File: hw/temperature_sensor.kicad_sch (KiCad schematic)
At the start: 8 parts, among them U103 DS18B20

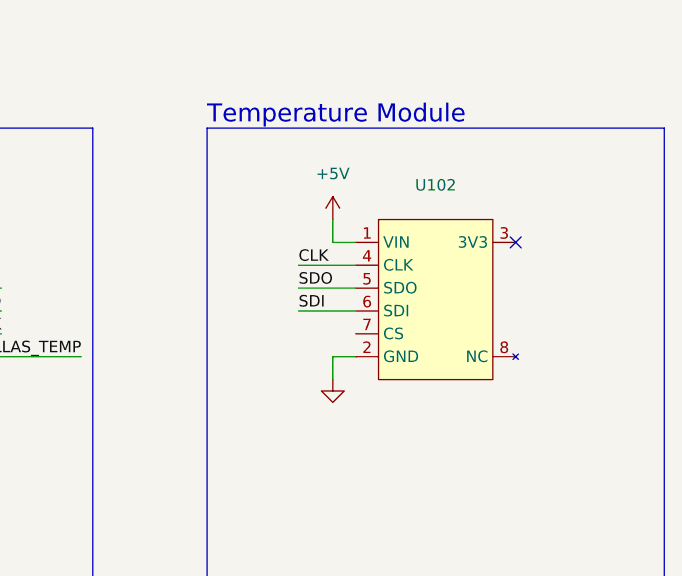
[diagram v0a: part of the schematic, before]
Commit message: schematic corrections & pcb routed
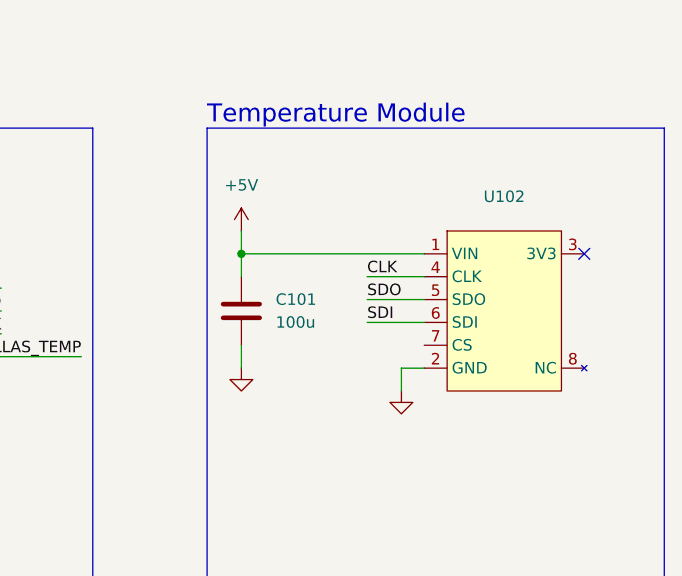
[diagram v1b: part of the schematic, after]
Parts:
- added C101: 100u, Capacitor_THT:CP_Radial_D5.0mm_P2.50mm, symbol Device:C
- U103: footprint Package_TO_SOT_THT:TO-92_Inline -> Connector_PinHeader_2.54mm:PinHeader_1x03_P2.54mm_Horizontal
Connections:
- net +5V: now also C101.1
- net GND: now also C101.2
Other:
- moved on the sheet: U102
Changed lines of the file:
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@@
 	(paper "A4")
+	(junction
+		(at 92.71 77.47)
+		(diameter 0)
+		(color 0 0 0 0)
+	)
 	(junction
 		(at 54.61 149.86)
@@
 	)
 	(no_connect
-		(at 123.19 76.2)
+		(at 130.81 77.47)
 	)
 	(no_connect
@@
 	(wire
 		(pts
-			(xy 99.06 78.74) (xy 105.41 78.74)
-		)
-		(stroke
-			(width 0)
-			(type default)
-		)
-	)
-	(wire
-		(pts
-			(xy 99.06 81.28) (xy 105.41 81.28)
+			(xy 106.68 80.01) (xy 113.03 80.01)
+		)
+		(stroke
+			(width 0)
+			(type default)
+		)
+	)
+	(wire
+		(pts
+			(xy 92.71 90.17) (xy 92.71 87.63)
+		)
+		(stroke
+			(width 0)
+			(type default)
+		)
+	)
+	(wire
+		(pts
+			(xy 92.71 77.47) (xy 113.03 77.47)
+		)
+		(stroke
+			(width 0)
+			(type default)
+		)
+	)
+	(wire
+		(pts
+			(xy 106.68 82.55) (xy 113.03 82.55)
 		)
 		(stroke
@@
 	(wire
 		(pts
-			(xy 102.87 73.66) (xy 102.87 76.2)
-		)
-		(stroke
-			(width 0)
-			(type default)
-		)
-	)
-	(wire
-		(pts
 			(xy 44.45 160.02) (xy 44.45 157.48)
 		)
@@
 	(wire
 		(pts
+			(xy 92.71 77.47) (xy 92.71 74.93)
+		)
+		(stroke
+			(width 0)
+			(type default)
+		)
+	)
+	(wire
+		(pts
 			(xy 62.23 76.2) (xy 59.69 76.2)
 		)
@@
 	(wire
 		(pts
-			(xy 102.87 91.44) (xy 102.87 88.9)
+			(xy 110.49 92.71) (xy 110.49 90.17)
 		)
 		(stroke
@@
 	(wire
 		(pts
-			(xy 99.06 83.82) (xy 105.41 83.82)
-		)
-		(stroke
-			(width 0)
-			(type default)
-		)
-	)
-	(wire
-		(pts
-			(xy 102.87 88.9) (xy 105.41 88.9)
+			(xy 106.68 85.09) (xy 113.03 85.09)
+		)
+		(stroke
+			(width 0)
+			(type default)
+		)
+	)
+	(wire
+		(pts
+			(xy 110.49 90.17) (xy 113.03 90.17)
 		)
 		(stroke
@@
 	(wire
 		(pts
+			(xy 92.71 77.47) (xy 92.71 80.01)
+		)
+		(stroke
+			(width 0)
+			(type default)
+		)
+	)
+	(wire
+		(pts
 			(xy 59.69 81.28) (xy 66.04 81.28)
 		)
@@
 		(pts
 			(xy 39.37 73.66) (xy 39.37 76.2)
-		)
-		(stroke
-			(width 0)
-			(type default)
-		)
-	)
-	(wire
-		(pts
-			(xy 102.87 76.2) (xy 105.41 76.2)
 		)
 		(stroke
@@
 	)
 	(label "CLK"
-		(at 99.06 78.74 0)
+		(at 106.68 80.01 0)
 		(effects
 			(font
@@
 	)
 	(label "SDO"
-		(at 99.06 81.28 0)
+		(at 106.68 82.55 0)
 		(effects
 			(font
@@
 	)
 	(label "SDI"
-		(at 99.06 83.82 0)
+		(at 106.68 85.09 0)
 		(effects
 			(font
@@
 			)
 		)
-		(property "Footprint" "Package_TO_SOT_THT:TO-92_Inline"
+		(property "Footprint" "Connector_PinHeader_2.54mm:PinHeader_1x03_P2.54mm_Horizontal"
 			(at 19.05 156.21 0)
 			(effects
@@
 	(symbol
 		(lib_id "power:+5V")
-		(at 102.87 73.66 0)
+		(at 92.71 74.93 0)
 		(unit 1)
 		(exclude_from_sim no)
@@
 		(fields_autoplaced yes)
 		(property "Reference" "#PWR0104"
-			(at 102.87 77.47 0)
+			(at 92.71 78.74 0)
 			(effects
 				(font
@@
 		)
 		(property "Value" "+5V"
-			(at 102.87 68.58 0)
+			(at 92.71 69.85 0)
 			(effects
 				(font
@@
 		)
 		(property "Footprint" ""
-			(at 102.87 73.66 0)
+			(at 92.71 74.93 0)
 			(effects
 				(font
@@
 		)
 		(property "Datasheet" ""
-			(at 102.87 73.66 0)
+			(at 92.71 74.93 0)
 			(effects
 				(font
@@
 		)
 		(property "Description" "Power symbol creates a global label with name \"+5V\""
-			(at 102.87 73.66 0)
+			(at 92.71 74.93 0)
 			(effects
 				(font
@@
 	(symbol
 		(lib_id "power:GND")
-		(at 102.87 91.44 0)
+		(at 110.49 92.71 0)
 		(unit 1)
 		(exclude_from_sim no)
@@
 		(fields_autoplaced yes)
 		(property "Reference" "#PWR0105"
-			(at 102.87 97.79 0)
+			(at 110.49 99.06 0)
 			(effects
 				(font
@@
 		)
 		(property "Value" "GND"
-			(at 102.87 96.52 0)
+			(at 110.49 97.79 0)
 			(effects
 				(font
@@
 		)
 		(property "Footprint" ""
-			(at 102.87 91.44 0)
+			(at 110.49 92.71 0)
 			(effects
 				(font
@@
 		)
 		(property "Datasheet" ""
-			(at 102.87 91.44 0)
+			(at 110.49 92.71 0)
 			(effects
 				(font
@@
 		)
 		(property "Description" "Power symbol creates a global label with name \"GND\" , ground"
-			(at 102.87 91.44 0)
+			(at 110.49 92.71 0)
 			(effects
 				(font
@@
 				(path "/d1c078f0-e8c6-4381-8df5-9bbdd95d8ece"
 					(reference "#PWR0105")
+					(unit 1)
+				)
+			)
+		)
+	)
+	(symbol
+		(lib_id "Device:C")
+		(at 92.71 83.82 0)
+		(unit 1)
+		(exclude_from_sim no)
+		(in_bom yes)
+		(on_board yes)
+		(dnp no)
+		(fields_autoplaced yes)
+		(property "Reference" "C101"
+			(at 96.52 82.5499 0)
+			(effects
+				(font
+					(size 1.27 1.27)
+				)
+				(justify left)
+			)
+		)
+		(property "Value" "100u"
+			(at 96.52 85.0899 0)
+			(effects
+				(font
+					(size 1.27 1.27)
+				)
+				(justify left)
+			)
+		)
+		(property "Footprint" "Capacitor_THT:CP_Radial_D5.0mm_P2.50mm"
+			(at 93.6752 87.63 0)
+			(effects
+				(font
+					(size 1.27 1.27)
+				)
+				(hide yes)
+			)
+		)
+		(property "Datasheet" "~"
+			(at 92.71 83.82 0)
+			(effects
+				(font
+					(size 1.27 1.27)
+				)
+				(hide yes)
+			)
+		)
+		(property "Description" "Unpolarized capacitor"
+			(at 92.71 83.82 0)
+			(effects
+				(font
+					(size 1.27 1.27)
+				)
+				(hide yes)
+			)
+		)
+		(pin "1"
+		)
+		(pin "2"
+		)
+		(instances
+			(project ""
+				(path "/d1c078f0-e8c6-4381-8df5-9bbdd95d8ece"
+					(reference "C101")
 					(unit 1)
 				)
@@
 	(symbol
 		(lib_id "temperature_sensor_symbols:TEMP")
-		(at 114.3 73.66 0)
+		(at 121.92 74.93 0)
 		(unit 1)
 		(exclude_from_sim no)
@@
 		(fields_autoplaced yes)
 		(property "Reference" "U102"
-			(at 114.3 69.85 0)
+			(at 121.92 71.12 0)
 			(effects
 				(font
@@
 		)
 		(property "Value" "~"
-			(at 114.3 72.39 0)
+			(at 121.92 73.66 0)
 			(effects
 				(font
@@
 		)
 		(property "Footprint" "temperature_sensor_footprints:Temperature_module"
-			(at 114.3 73.66 0)
+			(at 121.92 74.93 0)
 			(effects
 				(font
@@
 		)
 		(property "Datasheet" ""
-			(at 114.3 73.66 0)
+			(at 121.92 74.93 0)
 			(effects
 				(font
@@
 		)
 		(property "Description" ""
-			(at 114.3 73.66 0)
+			(at 121.92 74.93 0)
 			(effects
 				(font
@@
 					(unit 1)
 				)
+			)
+		)
+	)
+	(symbol
+		(lib_id "power:GND")
+		(at 92.71 90.17 0)
+		(unit 1)
+		(exclude_from_sim no)
+		(in_bom yes)
+		(on_board yes)
+		(dnp no)
+		(fields_autoplaced yes)
+		(property "Reference" "#PWR0108"
+			(at 92.71 96.52 0)
+			(effects
+				(font
+					(size 1.27 1.27)
+				)
+				(hide yes)
+			)
+		)
+		(property "Value" "GND"
+			(at 92.71 95.25 0)
+			(effects
+				(font
+					(size 1.27 1.27)
+				)
+				(hide yes)
+			)
+		)
+		(property "Footprint" ""
+			(at 92.71 90.17 0)
+			(effects
+				(font
+					(size 1.27 1.27)
+				)
+				(hide yes)
+			)
+		)
+		(property "Datasheet" ""
+			(at 92.71 90.17 0)
+			(effects
+				(font
+					(size 1.27 1.27)
+				)
+				(hide yes)
+			)
+		)
+		(property "Description" "Power symbol creates a global label with name \"GND\" , ground"
+			(at 92.71 90.17 0)
+			(effects
+				(font
+					(size 1.27 1.27)
+				)
+				(hide yes)
+			)
+		)
+		(pin "1"
+		)
+		(instances
+			(project "temperature_sensor"
+				(path "/d1c078f0-e8c6-4381-8df5-9bbdd95d8ece"
+					(reference "#PWR0108")
+					(unit 1)
+				)

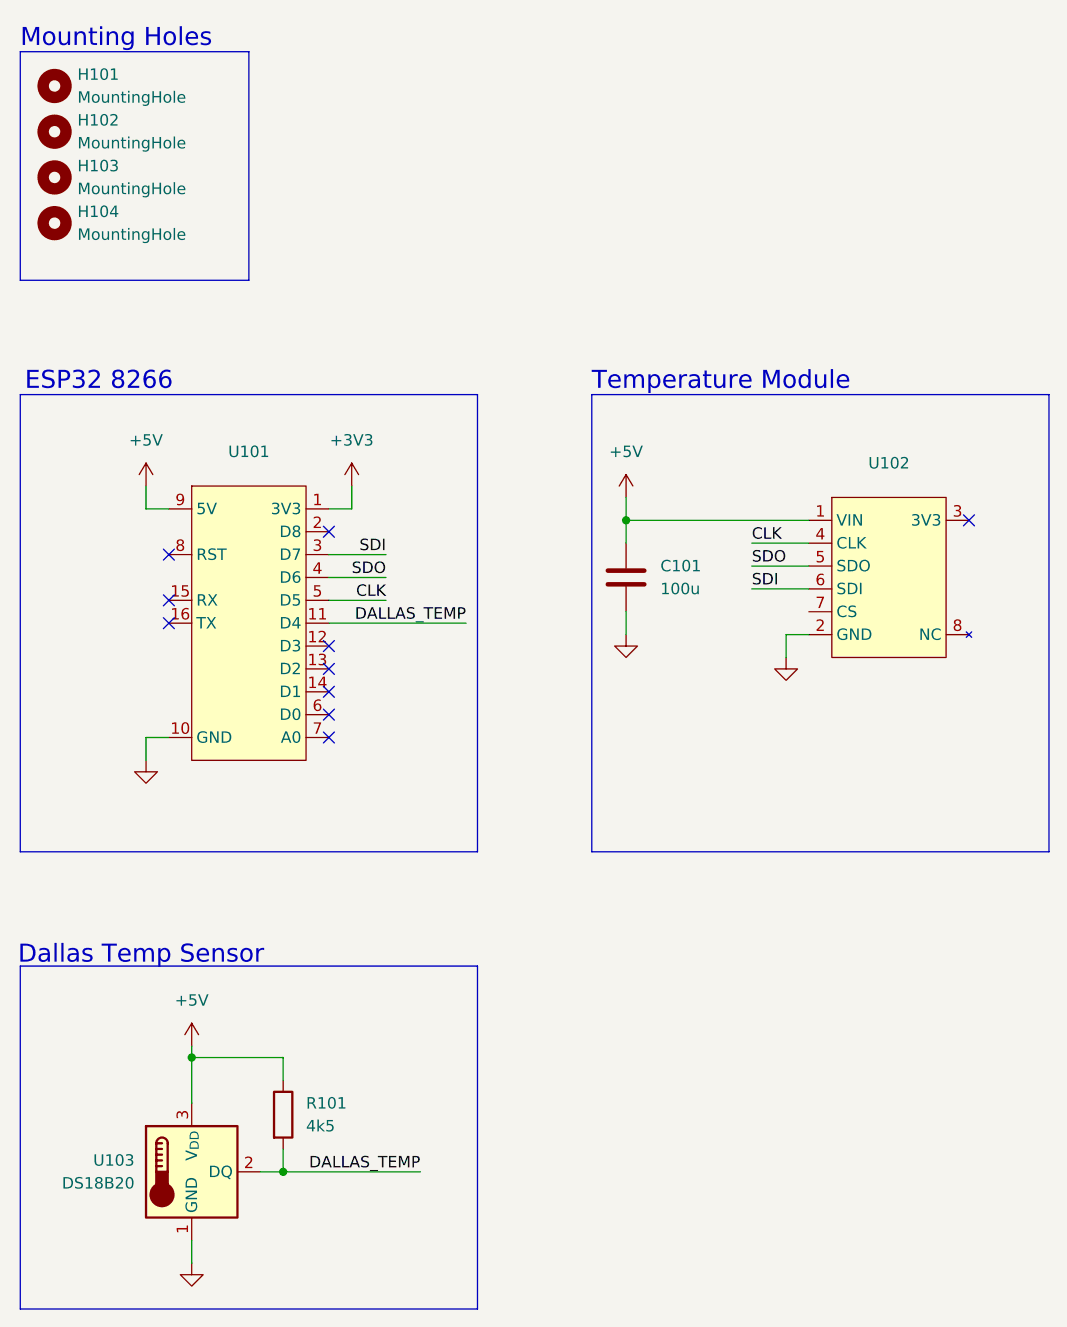
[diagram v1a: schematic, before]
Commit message: fixed CS form PT100 module
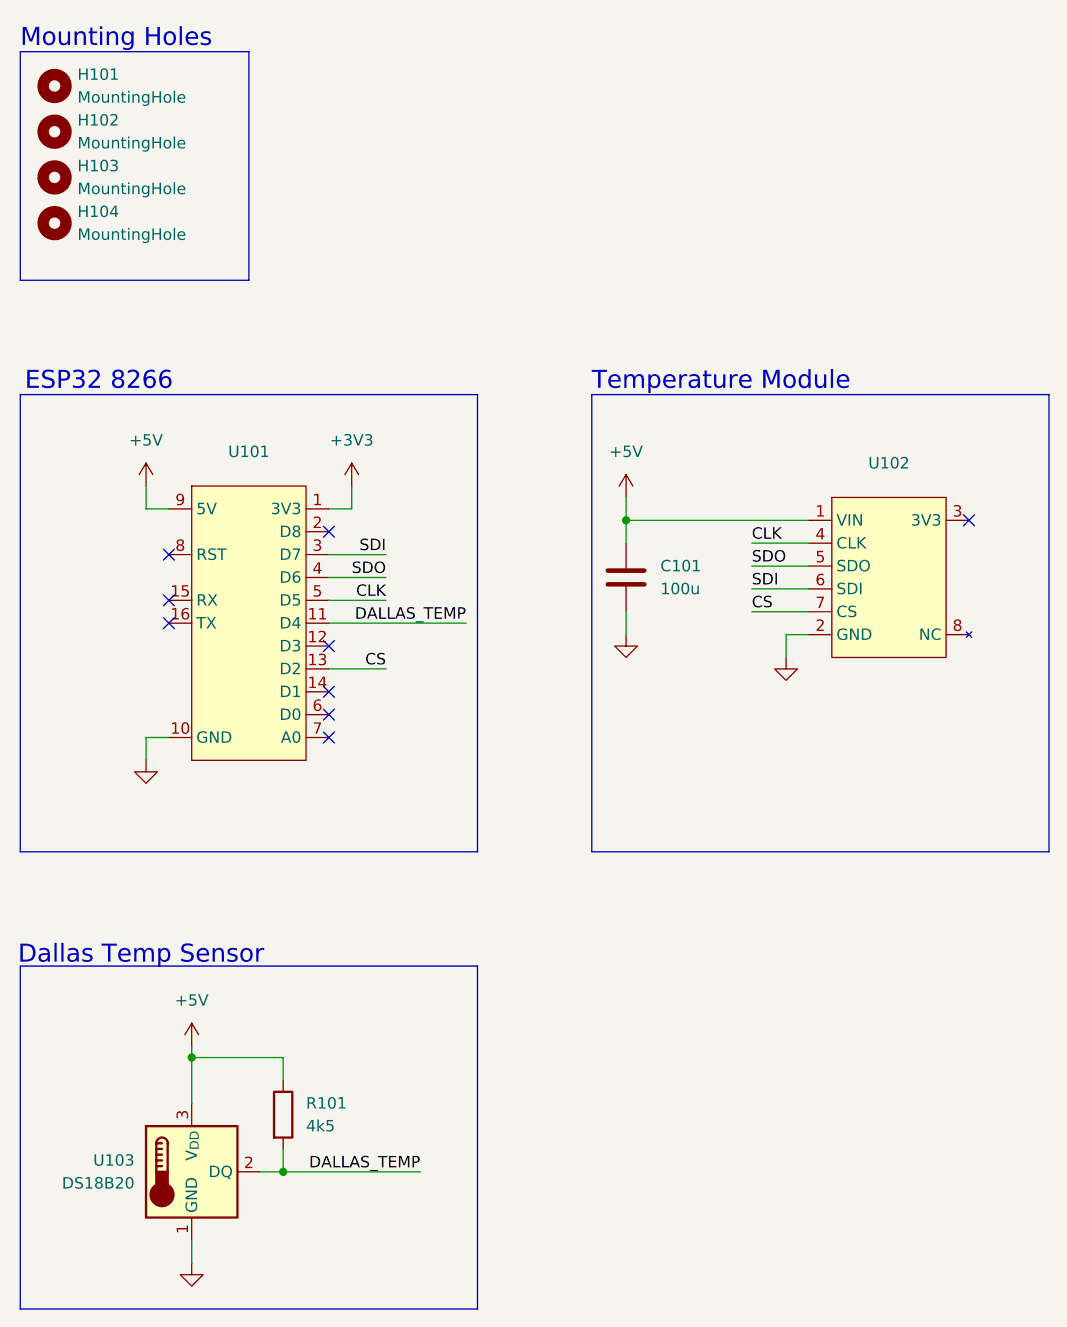
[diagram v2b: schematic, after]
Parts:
- R101: footprint Resistor_THT:R_Axial_DIN0204_L3.6mm_D1.6mm_P5.08mm_Horizontal -> Resistor_THT:R_Axial_DIN0204_L3.6mm_D1.6mm_P7.62mm_Horizontal
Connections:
- net CS: now reaches U101.13 (D2)
- net CS: now also U102.7 (CS)
- no-connect marks 10 -> 9
